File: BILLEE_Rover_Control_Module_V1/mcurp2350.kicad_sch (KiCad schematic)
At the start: 51 parts, among them J1 2.54mm Header, SW2 KMR2, SW3 RESET SW, U15 W25Q128JVSIQTR, U16 SN74LVC244APWR, U17 ABM8-272-T3_C20625731, U18 RP2350A_C42411118, U19 SN74LVC244APWR, U21 TCA4307DGKR, U22 TCA4307DGKR

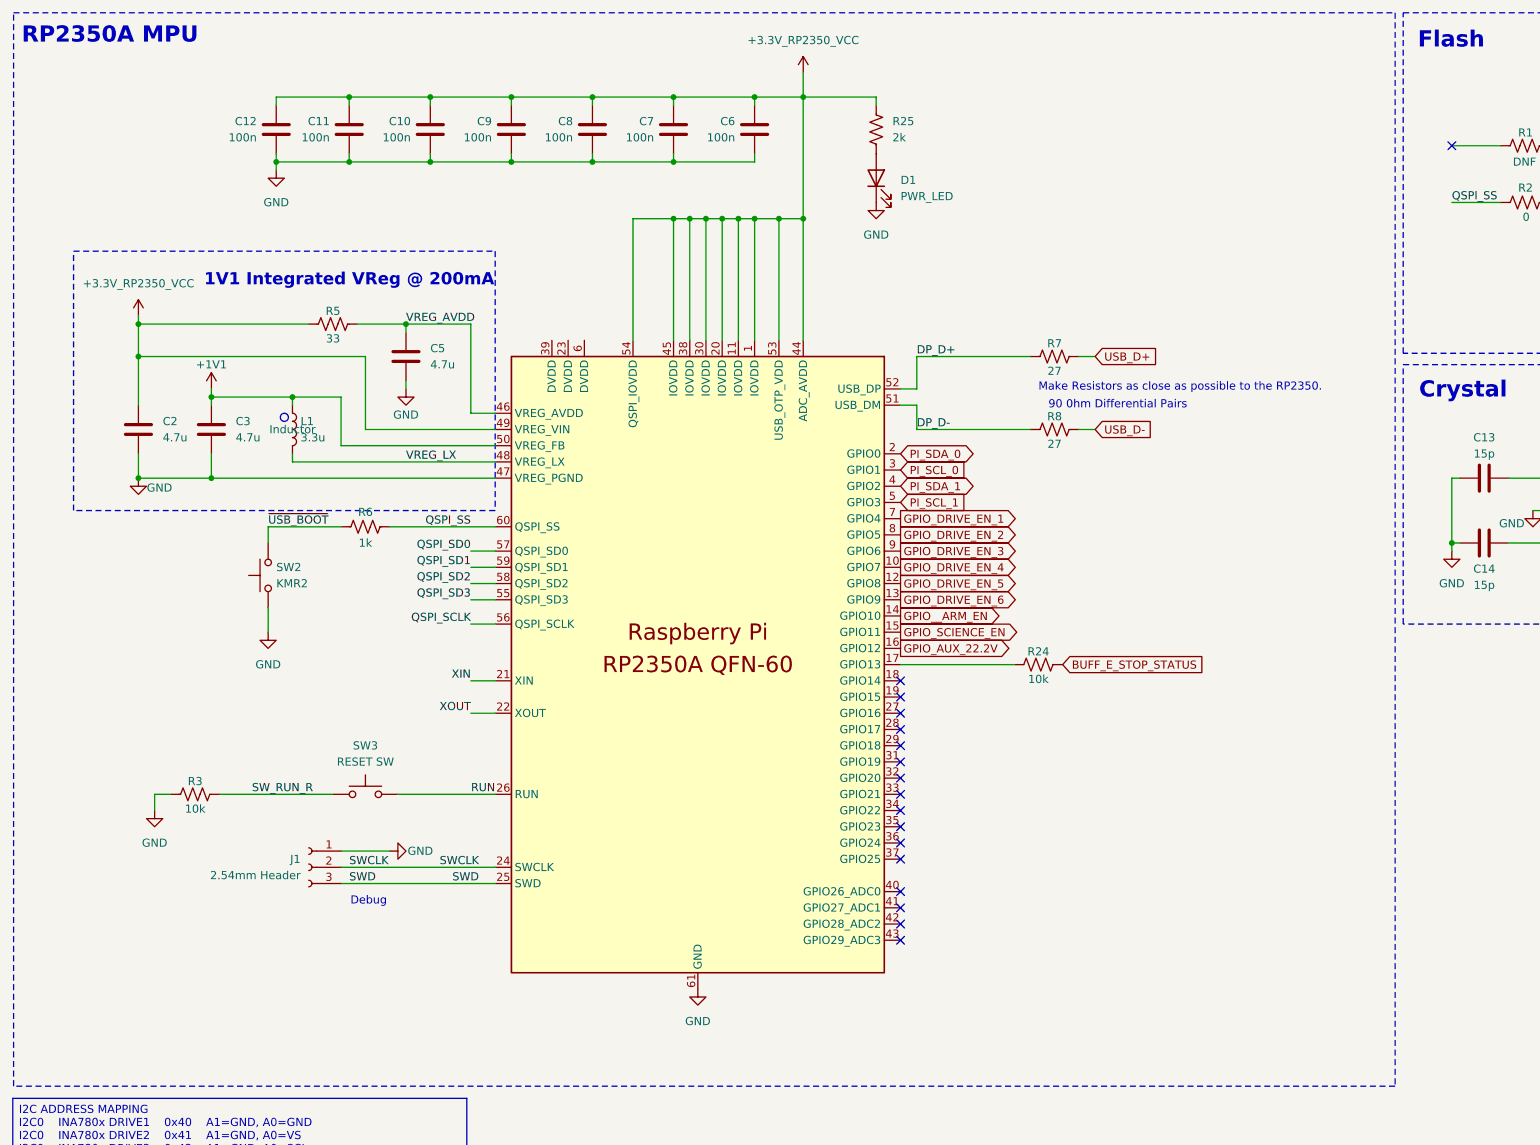
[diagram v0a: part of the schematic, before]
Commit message: Updated Firmware to running state and Fixed Missing pins on RP2350
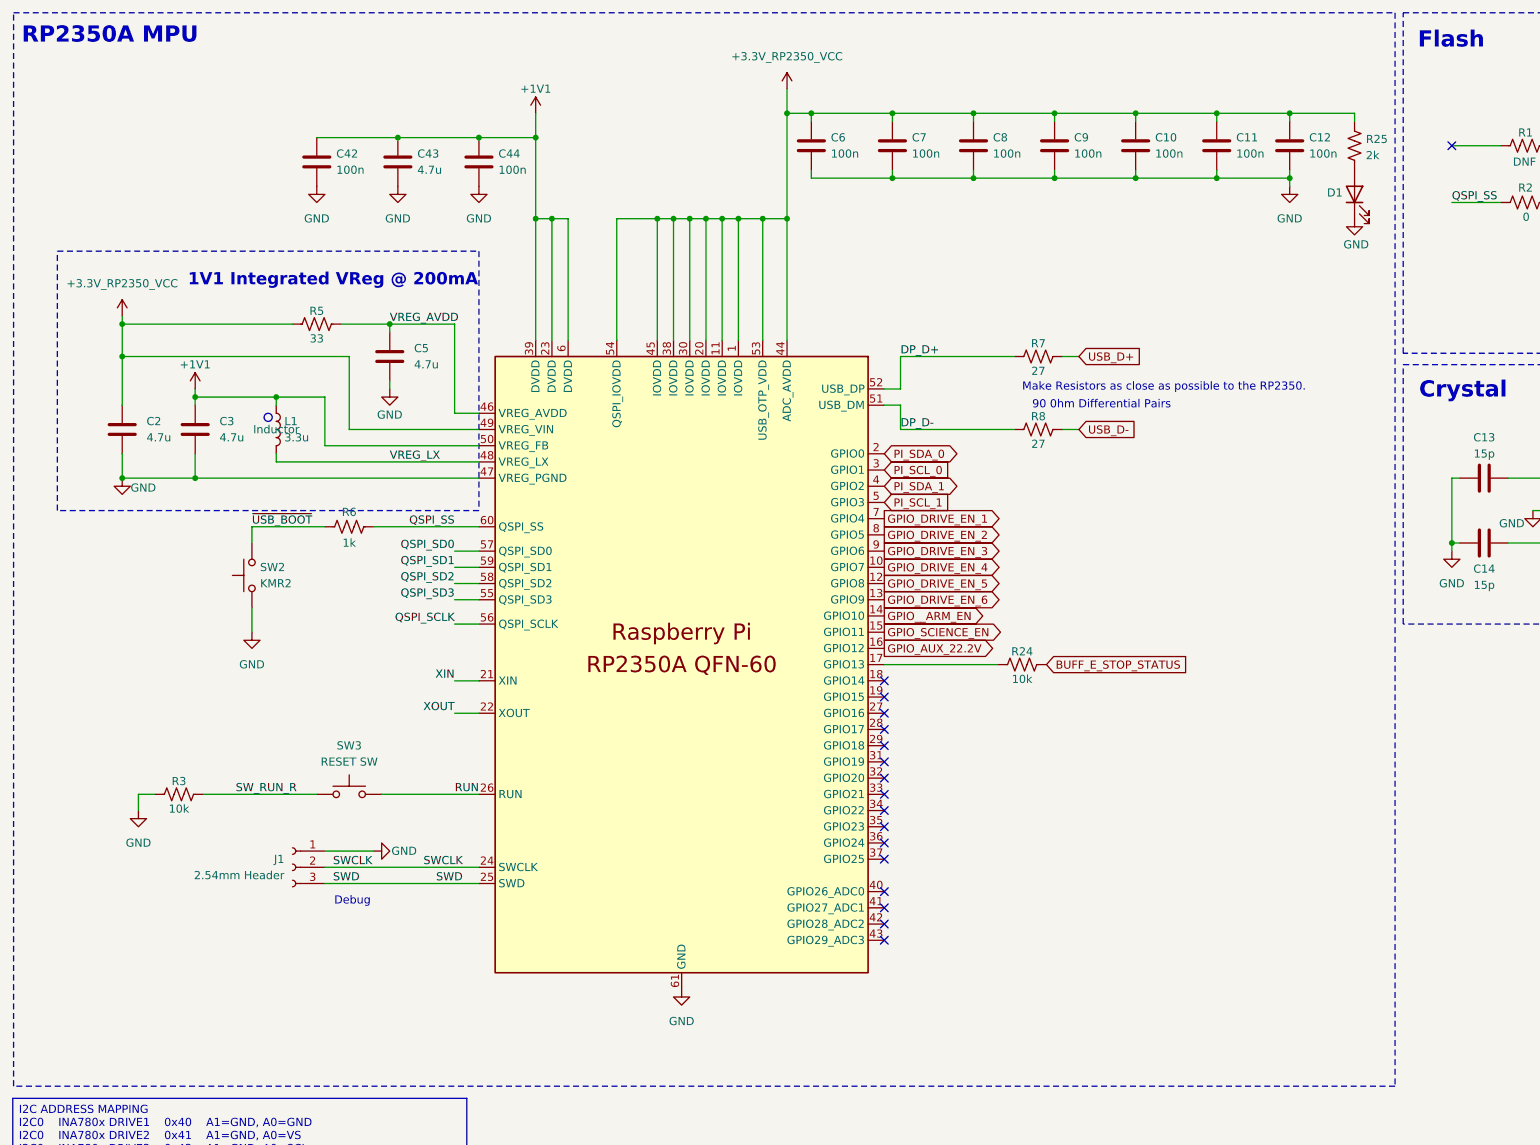
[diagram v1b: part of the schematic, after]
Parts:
- added C42, C44: 100n, Capacitor_SMD:C_0402_1005Metric, symbol Device:C
- added C43: 4.7u, Capacitor_SMD:C_0402_1005Metric, symbol Device:C
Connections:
- net +1V1: now also U18.23 (DVDD), U18.39 (DVDD), U18.6 (DVDD), C42.1, C43.1, C44.1
- net GND: now also C42.2, C43.2, C44.2
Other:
- moved on the sheet: C10, C11, C12, C2, C3, C5, C6, C7, C8, C9, D1, J1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
